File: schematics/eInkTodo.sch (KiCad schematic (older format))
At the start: 39 parts

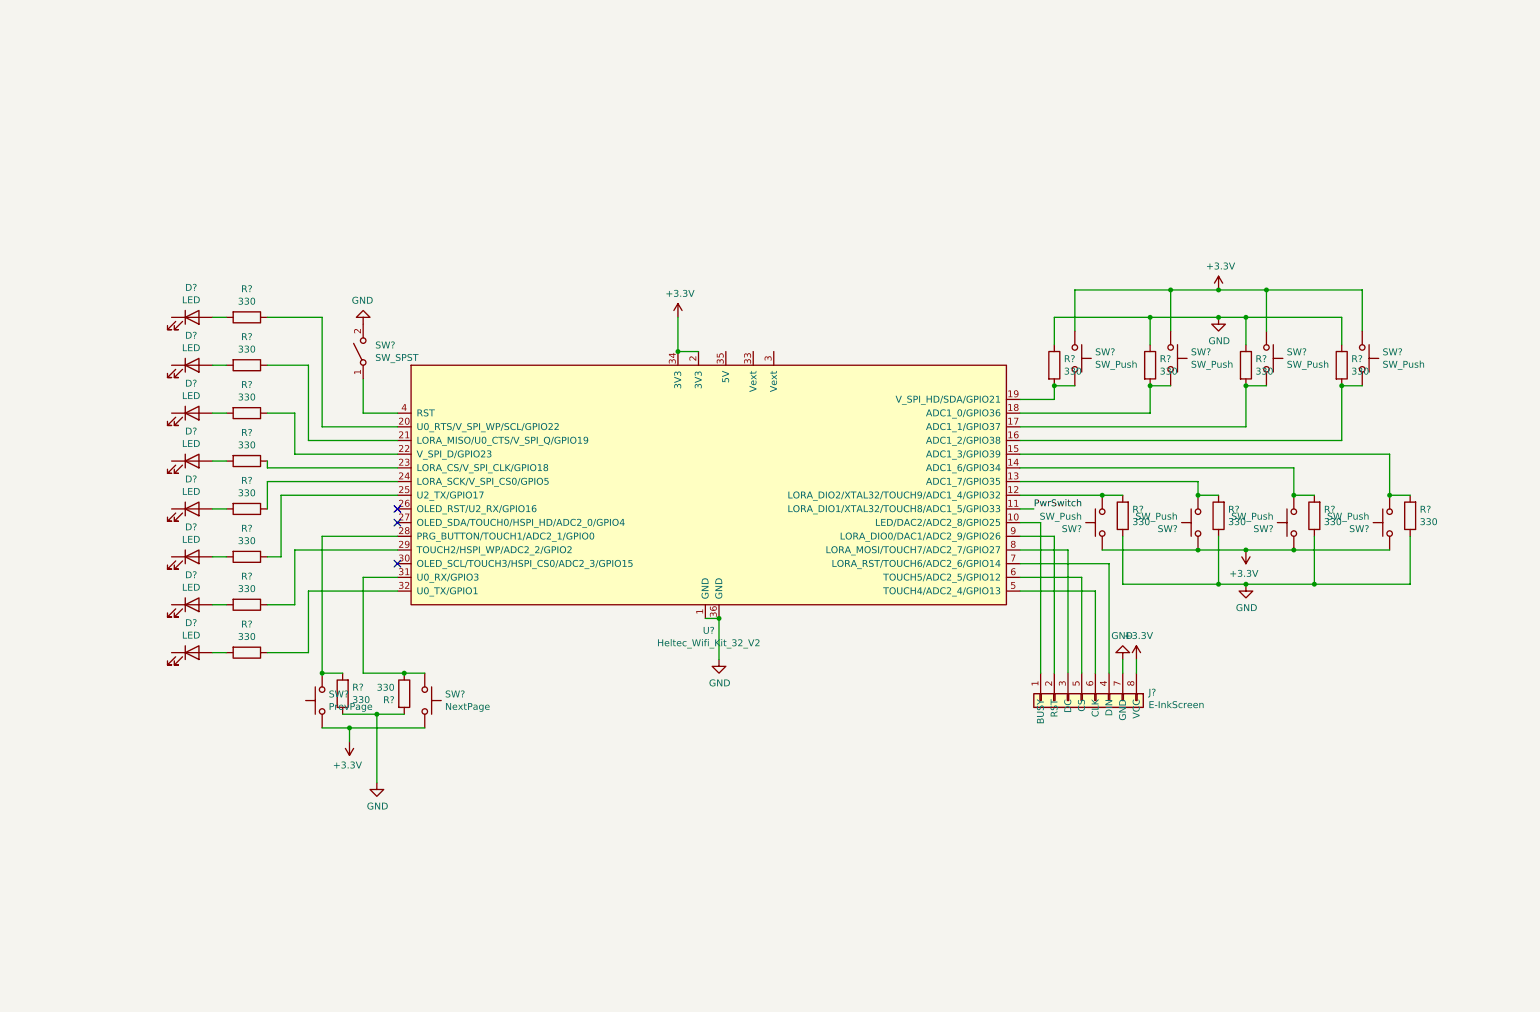
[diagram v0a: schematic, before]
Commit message: Almost complete schematic. Use Net labels for clarity. Add a buzzer
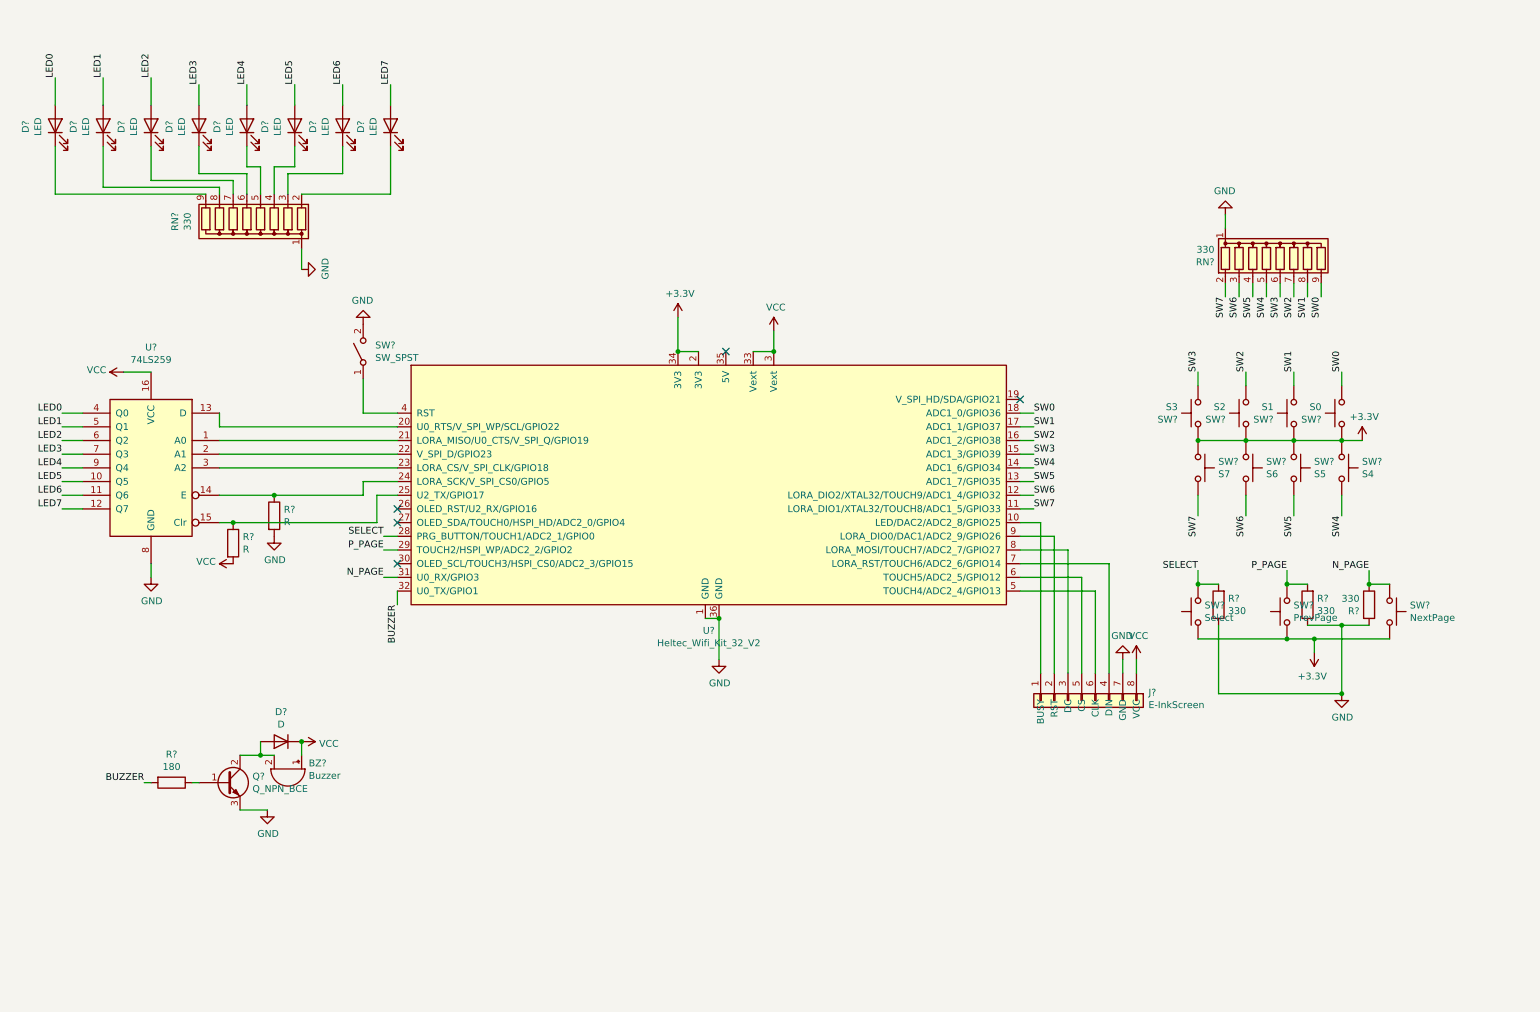
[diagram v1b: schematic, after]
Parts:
- removed R? (x16): 330, symbol Device:R
- removed SW? (x4): SW_Push, symbol Switch:SW_Push
- added BZ?: Buzzer, symbol Device:Buzzer
- added D?: D, symbol Device:D
- added Q?: Q_NPN_BCE, symbol Device:Q_NPN_BCE
- added R?: 180, symbol Device:R
- added R?: 330, symbol Device:R
- added R? (x2): R, symbol Device:R
- added RN? (x2): 330, Resistor_THT:R_Array_SIP9, symbol Device:R_Network08
- added SW?: S6, symbol Switch:SW_Push
- added SW?: S5, symbol Switch:SW_Push
- added SW?: S4, symbol Switch:SW_Push
- added SW?: S7, symbol Switch:SW_Push
- added SW?: Select, symbol Switch:SW_Push
- added U?: 74LS259, symbol 74xx:74LS259
- SW?: value SW_Push -> S0
- SW?: value SW_Push -> S1
- SW?: value SW_Push -> S2
- SW?: value SW_Push -> S3
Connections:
- net +3V3: now also SW?.1, SW?.1, SW?.1, SW?.1, SW?.1; no longer J?.8 (VCC)
- net GND: now also Q?.3 (E), R?.1, R?.2, RN?.1 (common), RN?.1 (common), U?.8 (GND)
- net SW6: now reaches U?.12 (LORA_DIO2/XTAL32/TOUCH9/ADC1_4/GPIO32)
- net SW6: now also RN?.3 (R2), SW?.2
- net SW5: now reaches U?.13 (ADC1_7/GPIO35)
- net SW5: now also RN?.4 (R3), SW?.2
- net SW4: now reaches U?.14 (ADC1_6/GPIO34)
- net SW4: now also RN?.5 (R4), SW?.2
- net SW3: now reaches U?.15 (ADC1_3/GPIO39)
- net SW3: now also SW?.2, RN?.6 (R5)
- net SW2: now reaches U?.16 (ADC1_2/GPIO38)
- net SW2: now also SW?.2, RN?.7 (R6); no longer SW?.2
- net SW1: now reaches U?.17 (ADC1_1/GPIO37)
- net SW1: now also SW?.2, RN?.8 (R7); no longer SW?.2
- net SW0: now reaches U?.18 (ADC1_0/GPIO36)
- net SW0: now also SW?.2, RN?.9 (R8); no longer SW?.2
- net at U?.19 (V_SPI_HD/SDA/GPIO21): no longer SW?.2
- net at U?.20 (U0_RTS/V_SPI_WP/SCL/GPIO22): now also U?.13 (D)
- net at U?.21 (LORA_MISO/U0_CTS/V_SPI_Q/GPIO19): now also U?.1 (A0)
- net at U?.22 (V_SPI_D/GPIO23): now also U?.2 (A1)
- net at U?.23 (LORA_CS/V_SPI_CLK/GPIO18): now also U?.3 (A2)
- net at U?.24 (LORA_SCK/V_SPI_CS0/GPIO5): now also R?.1, U?.14 (E)
- net at U?.25 (U2_TX/GPIO17): now also R?.1, U?.15 (Clr)
- net P_PAGE: now reaches R?.2, SW?.2
- net P_PAGE: now also U?.29 (TOUCH2/HSPI_WP/ADC2_2/GPIO2); no longer U?.28 (PRG_BUTTON/TOUCH1/ADC2_1/GPIO0)
- net VCC: now reaches U?.3 (Vext)
- net VCC: now also J?.8 (VCC), U?.33 (Vext), BZ?.1 (-), D?.1 (K), R?.2, U?.16 (VCC)
- net N_PAGE: now reaches R?.1, SW?.1, U?.31 (U0_RX/GPIO3)
- net BUZZER: now reaches U?.32 (U0_TX/GPIO1)
- net BUZZER: now also R?.2
- net at D?.1 (K): now also RN?.9 (R8)
- net LED0: now reaches D?.2 (A)
- net LED0: now also U?.4 (Q0)
- net at D?.1 (K): now also RN?.8 (R7)
- net LED1: now reaches D?.2 (A)
- net LED1: now also U?.5 (Q1)
- net at D?.1 (K): now also RN?.7 (R6)
- net LED2: now reaches D?.2 (A)
- net LED2: now also U?.6 (Q2)
- net at D?.1 (K): now also RN?.6 (R5)
- net LED3: now reaches D?.2 (A)
- net LED3: now also U?.7 (Q3)
- net at D?.1 (K): now also RN?.5 (R4)
- net LED4: now reaches D?.2 (A)
- net LED4: now also U?.9 (Q4)
- net at D?.1 (K): now also RN?.4 (R3)
- net LED5: now reaches D?.2 (A)
- net LED5: now also U?.10 (Q5)
- net at D?.1 (K): now also RN?.3 (R2)
- net LED6: now reaches D?.2 (A)
- net LED6: now also U?.11 (Q6)
- net at D?.1 (K): now also RN?.2 (R1)
- net LED7: now reaches D?.2 (A)
- net LED7: now also U?.12 (Q7)
- net PwrSwitch renamed SW7
- net SW7: now also RN?.2 (R1), SW?.2
- new net: BZ?.2 (+), D?.2 (A), Q?.2 (C)
- new net: Q?.1 (B), R?.1
- new net SELECT: R?.2, SW?.2, U?.28 (PRG_BUTTON/TOUCH1/ADC2_1/GPIO0)
- no-connect marks 3 -> 5
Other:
- moved on the sheet: D?, R?, SW?

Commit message: Finish board layout
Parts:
- removed D? (x8): LED, symbol Device:LED
- removed RN?: 330, Resistor_THT:R_Array_SIP9, symbol Device:R_Network08
- removed SW?: S0, symbol Switch:SW_Push
- removed SW?: S1, symbol Switch:SW_Push
- removed SW?: S2, symbol Switch:SW_Push
- removed SW?: S3, symbol Switch:SW_Push
- removed SW?: PrevPage, symbol Switch:SW_Push
- removed SW?: NextPage, symbol Switch:SW_Push
- removed SW?: S6, symbol Switch:SW_Push
- removed SW?: S5, symbol Switch:SW_Push
- removed SW?: S4, symbol Switch:SW_Push
- removed SW?: S7, symbol Switch:SW_Push
- removed SW?: Select, symbol Switch:SW_Push
- added 3v3: BREAD 3v3, Connector_PinHeader_2.54mm:PinHeader_1x04_P2.54mm_Vertical, symbol Connector_Generic:Conn_01x04
- added GND: BREAD GND, Connector_PinHeader_2.54mm:PinHeader_1x04_P2.54mm_Vertical, symbol Connector_Generic:Conn_01x04
- added H1, H3, H4: MountingHole, MountingHole:MountingHole_2.7mm_M2.5, symbol Mechanical:MountingHole
- added J2, J3, J4, J5: BREADBOARD, Connector_PinHeader_2.54mm:PinHeader_1x36_P2.54mm_Vertical, symbol Connector_Generic:Conn_01x36
- added LED_CONN1: Conn_01x08, Connector_PinHeader_2.54mm:PinHeader_1x08_P2.54mm_Horizontal, symbol Connector_Generic:Conn_01x08
- added POWER_CONN1: Conn_01x02, Connector_PinHeader_2.54mm:PinHeader_1x02_P2.54mm_Horizontal, symbol Connector_Generic:Conn_01x02
- added R10, R11, R12, R13, R14, R7, R8, R9: 330, Resistor_THT:R_Axial_DIN0207_L6.3mm_D2.5mm_P10.16mm_Horizontal, symbol Device:R
- added SWITCH_CONN1: Conn_01x08, Connector_PinHeader_2.54mm:PinHeader_1x11_P2.54mm_Horizontal, symbol Connector_Generic:Conn_01x11
- BZ1: renamed from BZ?; footprint (none) -> Buzzer_Beeper:MagneticBuzzer_CUI_CST-931RP-A
- D6: renamed from D?; footprint (none) -> Diode_THT:D_DO-41_SOD81_P10.16mm_Horizontal
- EINK_CONN: renamed from J?; footprint (none) -> Connector_PinHeader_2.54mm:PinHeader_1x08_P2.54mm_Horizontal
- Q1: renamed from Q?; footprint (none) -> Package_TO_SOT_THT:TO-92_HandSolder
- R1, R2, R3, R4, R5, R6: renamed from R?; footprint (none) -> Resistor_THT:R_Axial_DIN0207_L6.3mm_D2.5mm_P10.16mm_Horizontal
- SW1: renamed from SW?; footprint (none) -> Connector_PinHeader_2.54mm:PinHeader_1x02_P2.54mm_Vertical
- U1: renamed from U?; footprint (none) -> Package_DIP:DIP-16_W7.62mm_LongPads
- gave numbers to parts that had none: 2
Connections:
- net +3V3: now also BZ1.1 (-), D6.1 (K), R2.2, U1.16 (VCC), 3v3.1 (Pin_1), 3v3.2 (Pin_2), 3v3.3 (Pin_3), 3v3.4 (Pin_4), POWER_CONN1.1 (Pin_1)
- net GND: now also GND.1 (Pin_1), GND.2 (Pin_2), GND.3 (Pin_3), GND.4 (Pin_4), POWER_CONN1.2 (Pin_2)
- net LED0: now also U1.7 (Q3), R7.1; no longer U1.4 (Q0)
- net LED1: now also U1.6 (Q2), R8.1; no longer U1.5 (Q1)
- net LED2: now also U1.5 (Q1), R9.1; no longer U1.6 (Q2)
- net LED3: now also U1.4 (Q0), R10.1; no longer U1.7 (Q3)
- net LED4: now also R11.1
- net LED5: now also R12.1
- net LED6: now also R13.1
- net LED7: now also R14.1
- net N_PAGE: now also SWITCH_CONN1.11 (Pin_11)
- net P_PAGE: now also SWITCH_CONN1.10 (Pin_10)
- net SELECT: now also SWITCH_CONN1.9 (Pin_9)
- net SW0: now also SWITCH_CONN1.1 (Pin_1)
- net SW1: now also SWITCH_CONN1.2 (Pin_2)
- net SW2: now also SWITCH_CONN1.3 (Pin_3)
- net SW3: now also SWITCH_CONN1.4 (Pin_4)
- net SW4: now also SWITCH_CONN1.5 (Pin_5)
- net SW5: now also SWITCH_CONN1.6 (Pin_6)
- net SW6: now also SWITCH_CONN1.7 (Pin_7)
- net SW7: now also SWITCH_CONN1.8 (Pin_8)
- net VCC: no longer BZ1.1 (-), D6.1 (K), R2.2, U1.16 (VCC)
- net at U2.21 (LORA_MISO/U0_CTS/V_SPI_Q/GPIO19): now also U1.3 (A2); no longer U1.1 (A0)
- net at U2.23 (LORA_CS/V_SPI_CLK/GPIO18): now also U1.1 (A0); no longer U1.3 (A2)
- new net: LED_CONN1.2 (Pin_2), R8.2
- new net: LED_CONN1.1 (Pin_1), R7.2
- new net: LED_CONN1.3 (Pin_3), R9.2
- new net: LED_CONN1.4 (Pin_4), R10.2
- new net: LED_CONN1.5 (Pin_5), R11.2
- new net: LED_CONN1.6 (Pin_6), R12.2
- new net: LED_CONN1.7 (Pin_7), R13.2
- new net: LED_CONN1.8 (Pin_8), R14.2
- no-connect marks 5 -> 149
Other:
- moved on the sheet: BZ1, D6, Q1, R1, R4, R5, R6

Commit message: Update pin #s
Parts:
- renumbered EINK_CONN to EINK_CONN1, GND to GND1
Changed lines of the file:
@@
 N_PAGE
 $Comp
-L schematics:E-InkScreen EINK_CONN
+L schematics:E-InkScreen EINK_CONN1
 U 1 1 608B208A
 P 8500 5550
-F 0 "EINK_CONN" V 8441 5938 50  0000 L CNN
+F 0 "EINK_CONN1" V 8441 5938 50  0000 L CNN
 F 1 "E-InkScreen" V 8532 5938 50  0000 L CNN
 F 2 "Connector_PinHeader_2.54mm:PinHeader_1x08_P2.54mm_Horizontal" H 8500 5550 50  0001 C CNN
@@
 $EndComp
 $Comp
-L Connector_Generic:Conn_01x04 GND
+L Connector_Generic:Conn_01x04 GND1
 U 1 1 60FA9AE0
 P 5000 6500
-F 0 "GND" V 4872 6680 50  0000 L CNN
+F 0 "GND1" V 4872 6680 50  0000 L CNN
 F 1 "BREAD GND" V 4963 6680 50  0000 L CNN
 F 2 "Connector_PinHeader_2.54mm:PinHeader_1x04_P2.54mm_Vertical" H 5000 6500 50  0001 C CNN
